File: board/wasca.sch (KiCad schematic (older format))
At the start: 104 parts, among them CN1 CARTRIDGE_EDGE_CONNECTOR, CN2 TFP09-2-12B, CN3 Conn_02x02_Odd_Even, CN4 Conn_02x02_Odd_Even, CN5 Conn_02x03_Odd_Even, CN6 USB-MB-S, CN7 Conn_02x05_Odd_Even, SW1 Conn_01x03_Male, U1 74ALVC164245, U10 SN74LVC1T45DBV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

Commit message: Finalizing stuff for 1.4: cleanup, silkscreen, comments etc.
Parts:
- removed CN6: USB-MB-S, con-usb-USB-MB-S, symbol USB-MB-S:USB-MB-S
- removed U13: ESP32_CAM, wasca:MODULE_ESP32-CAM, symbol esp32-devkitc:ESP32_CAM
- added CHAMFER_WARN1, CHAMFER_WARN2: CHAMFER_WARNING, wasca:CHAMFER_WARNING, symbol wasca:CHAMFER_WARNING
- added CN6: USB_C_Receptacle_USB2.0, wasca:DX07S016JA1R1500, symbol Connector:USB_C_Receptacle_USB2.0
- added R20: 5K1, Capacitor_SMD:C_0603_1608Metric_Pad1.08x0.95mm_HandSolder, symbol Device:R
- added U13: ESP32_CAM_HALF, wasca:MODULE_ESP32-CAM-HALF, symbol esp32-devkitc:ESP32_CAM_HALF
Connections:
- wire segments 878 -> 890
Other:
- note added: "Compatible connectors:\nHroparts TF-01A\nSOFNG TF-15x15\nSOFNG TF-015\nXUNPU TF-115K\nXUNPU TF-109\nHOAUC HYC77-TF09-200"
- note added: "Compatible connectors:\nJAE DX07S016JA1R1500\nJAE DX07S016JA3R1500\nHROPARTS TYPE-C-31-M-12\nHROPARTS TYPE-C-31-M-14\nXKB U262-161N-4BVC11\nJing Ext. C167321"
- note added: "Partially compatible\n(signals only)\n\nHirose DM3AT-SF-PEJM5\nKyocera 045138008100858+\nYamaichi PJS008-4100-0-VE"
- note removed: "TODO: add footprint to help orientation for 3V3 buffers\nTODO: pin B45 isn't A0 and consequently all address pins must be shifted and re-routed.\nTODO: restrict address lines count to A0-A23 (no plan to use A24)\nTODO: Use PLL output pin (32 or 33) for SDRAM clock. Probably requires to change SDRAM chip orientation.\nTODO: Change JTAG connector orientation, in order to support pokayoke connector.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"
- moved on the sheet: R13, R14

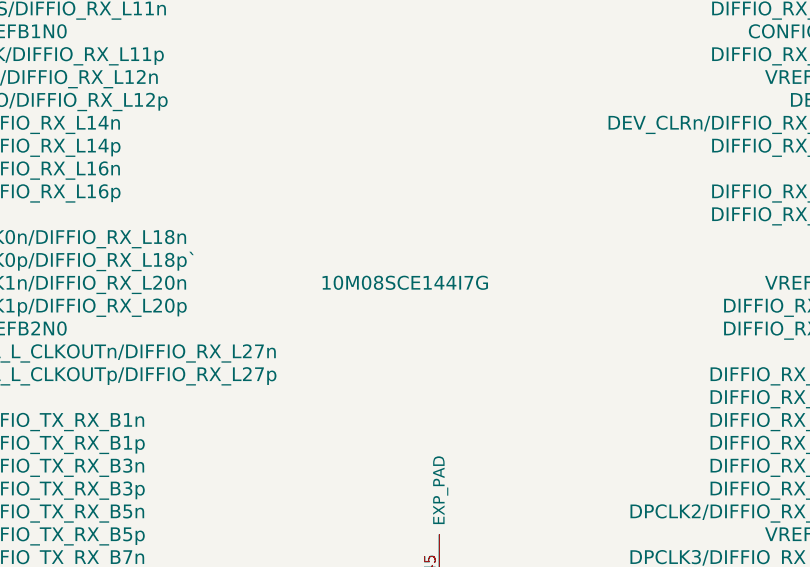
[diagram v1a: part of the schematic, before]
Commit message: Changing FPGA part to 10M08SCE144C8G. BOM recompilation.
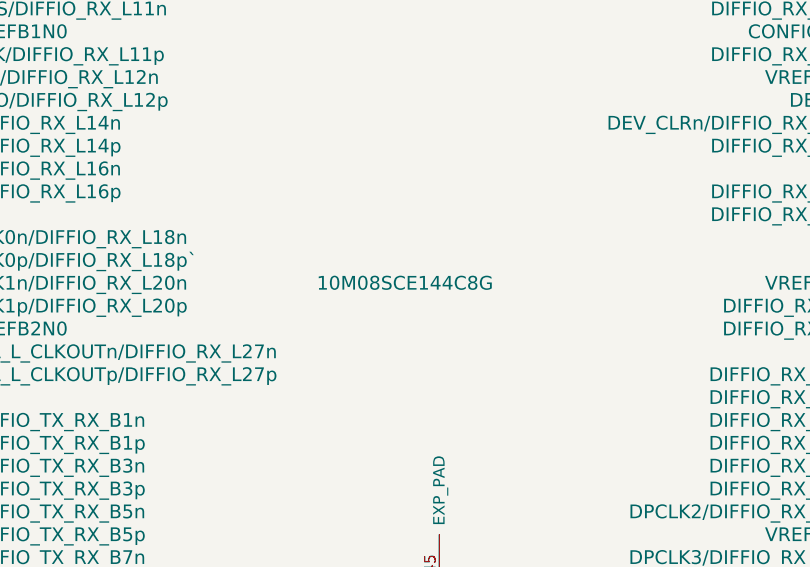
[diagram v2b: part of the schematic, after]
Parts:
- U3: value 10M08SCE144I7G -> 10M08SCE144C8G
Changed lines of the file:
@@
 P 25450 6500
 F 0 "U3" H 27500 9700 60  0000 C CNN
-F 1 "10M08SCE144I7G" H 25450 6800 60  0000 C CNN
+F 1 "10M08SCE144C8G" H 25450 6800 60  0000 C CNN
 F 2 "wasca:TQFP144_ALTERA_HANDSOLDERING" H 25450 6100 60  0001 C CNN
 F 3 "" H 25100 6500 60  0000 C CNN

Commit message: SSEL pin duplicated to STM32
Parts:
- added R21: 0, Capacitor_SMD:C_0603_1608Metric_Pad1.08x0.95mm_HandSolder, symbol Device:R
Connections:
- wire segments 890 -> 892

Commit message: Board 1.5 update (unchecked)
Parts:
- added R22, R23: 0, Capacitor_SMD:C_0603_1608Metric_Pad1.08x0.95mm_HandSolder, symbol Device:R
- added R24: 470, Capacitor_SMD:C_0603_1608Metric_Pad1.08x0.95mm_HandSolder, symbol Device:R
- SW1: footprint wasca:NINJA_SW -> Connector_PinHeader_2.54mm:PinHeader_1x03_P2.54mm_Vertical
- U6: footprint Package_QFP:LQFP-64_10x10mm_P0.5mm -> wasca:LQFP-64_10x10mm_P0.5mm
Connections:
- net labels added: 5V_SATURN_DETECT, BUFFERS_OE
- net labels removed: SPARE1, SPARE2
- wire segments 892 -> 889
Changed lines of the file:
@@
 Text Label 26400 14900 0    40   ~ 0
 LED3
-Text Label 26350 15000 0    40   ~ 0
-SPARE1
-Text Label 26350 15100 0    40   ~ 0
-SPARE2
 Text Notes 17850 10300 0    39   ~ 0
 SDRAM : shares 3V3 with MAX10\nDDR : requires 2V5 power supply
@@
 L power:GND #PWR065
 U 1 1 577FA6A0
-P 30050 15100
-F 0 "#PWR065" H 30050 14850 50  0001 C CNN
-F 1 "GND" H 30050 14950 50  0001 C CNN
-F 2 "" H 30050 15100 60  0000 C CNN
-F 3 "" H 30050 15100 60  0000 C CNN
-	1    30050 15100
+P 30400 15050
+F 0 "#PWR065" H 30400 14800 50  0001 C CNN
+F 1 "GND" H 30400 14900 50  0001 C CNN
+F 2 "" H 30400 15050 60  0000 C CNN
+F 3 "" H 30400 15050 60  0000 C CNN
+	1    30400 15050
 	1    0    0    -1
 $EndComp
@@
 	22450 2400 22600 2400
 Wire Wire Line
-	10150 3000 10250 3000
-Wire Wire Line
-	10150 3100 10250 3100
-Wire Wire Line
-	10250 3100 10250 3000
-Connection ~ 10250 3000
-Wire Wire Line
 	28850 4300 29250 4300
 Wire Wire Line
@@
 Connection ~ 16150 12050
 Wire Wire Line
-	9200 6950 9300 6950
-Wire Wire Line
 	22450 2900 23750 2900
 Wire Wire Line
@@
 Wire Wire Line
 	3650 14950 4400 14950
-Connection ~ 10250 1900
-Wire Wire Line
-	10250 2000 10250 1900
-Wire Wire Line
-	10150 2000 10250 2000
-Wire Wire Line
-	10150 1900 10250 1900
 Wire Wire Line
 	10150 3900 10900 3900
@@
 	18900 9950 17800 9950
 Wire Wire Line
-	29000 14900 30050 14900
+	29000 14900 30400 14900
 Wire Wire Line
-	30050 14900 30050 15000
+	30400 14900 30400 15000
 Wire Wire Line
-	29000 15000 30050 15000
-Connection ~ 30050 15000
+	29000 15000 30400 15000
+Connection ~ 30400 15000
 Wire Wire Line
 	15600 17300 15600 17450
@@
 	24750 2900 24850 2900
 Wire Wire Line
-	10250 3000 10850 3000
-Wire Wire Line
 	16150 12050 16550 12050
 Wire Wire Line
@@
 	8550 1600 8650 1600
 Wire Wire Line
-	10250 1900 10850 1900
-Wire Wire Line
 	9300 5550 10050 5550
 Wire Wire Line
@@
 	18250 9400 18600 9400
 Wire Wire Line
-	30050 15000 30050 15100
+	30400 15000 30400 15050
 Wire Wire Line
 	15600 17450 15600 17600
@@
 F 0 "U6" H 26000 11650 50  0000 C CNN
 F 1 "STM32F446RETx" H 26100 11500 50  0000 C CNN
-F 2 "Package_QFP:LQFP-64_10x10mm_P0.5mm" H 24900 11800 50  0001 R CNN
+F 2 "wasca:LQFP-64_10x10mm_P0.5mm" H 24900 11800 50  0001 R CNN
 F 3 "http://www.st.com/st-web-ui/static/active/en/resource/technical/document/datasheet/DM00141306.pdf" H 25500 13500 50  0001 C CNN
 	1    25500 13500
@@
 Wire Wire Line
 	9200 10800 10650 10800
-$Comp
-L power:GND #PWR047
-U 1 1 61E039AD
-P 9350 12000
-F 0 "#PWR047" H 9350 11750 50  0001 C CNN
-F 1 "GND" H 9350 11850 50  0000 C CNN
-F 2 "" H 9350 12000 60  0000 C CNN
-F 3 "" H 9350 12000 60  0000 C CNN
-	1    9350 12000
-	1    0    0    -1
-$EndComp
-Wire Wire Line
-	9200 12000 9350 12000
-$Comp
-L power:GND #PWR040
-U 1 1 61FB8A1A
-P 9350 10900
-F 0 "#PWR040" H 9350 10650 50  0001 C CNN
-F 1 "GND" H 9350 10750 50  0000 C CNN
-F 2 "" H 9350 10900 60  0000 C CNN
-F 3 "" H 9350 10900 60  0000 C CNN
-	1    9350 10900
-	1    0    0    -1
-$EndComp
-Wire Wire Line
-	9200 10900 9350 10900
 Wire Wire Line
 	9200 7550 10900 7550
@@
 Wire Wire Line
 	9200 7450 10900 7450
-Wire Wire Line
-	9200 7050 9300 7050
-Wire Wire Line
-	9300 7050 9300 6950
-Connection ~ 9300 6950
-Wire Wire Line
-	9300 6950 10800 6950
 $Comp
 L power:GND #PWR027
@@
 	1    0    0    -1
 $EndComp
-Wire Wire Line
-	9200 5850 9300 5850
-Wire Wire Line
-	9200 5950 9300 5950
-Wire Wire Line
-	9300 5950 9300 5850
-Connection ~ 9300 5850
-Wire Wire Line
-	9300 5850 10800 5850
 Text Label 11000 2400 0    40   ~ 0
 ABUS_3V_A1
@@
 DBG_UART_RX
 Wire Wire Line
-	29000 15100 29750 15100
-Text Label 29200 15100 0    40   ~ 0
+	29000 15100 29550 15100
+Text Label 29050 15100 0    40   ~ 0
 DBG_UART_TX
 Wire Wire Line
@@
 Text Label 27950 15100 0    40   ~ 0
 DBG_UART_RX
-Text Label 28200 15000 0    40   ~ 0
-SPARE1
-Text Label 28200 14900 0    40   ~ 0
-SPARE2
 Wire Wire Line
 	28500 15000 28100 15000
@@
 F 0 "SW1" H 23258 12481 50  0000 C CNN
 F 1 "Conn_01x03_Male" H 23258 12390 50  0000 C CNN
-F 2 "wasca:NINJA_SW" H 23150 12200 50  0001 C CNN
+F 2 "Connector_PinHeader_2.54mm:PinHeader_1x03_P2.54mm_Vertical" H 23150 12200 50  0001 C CNN
 F 3 "~" H 23150 12200 50  0001 C CNN
 	1    23150 12200
@@
 Wire Wire Line
 	26200 14100 27200 14100
-Wire Bus Line
-	2150 1400 2150 5850
-Wire Bus Line
-	6200 8300 6200 10600
-Wire Bus Line
-	3150 8300 3150 10600
-Wire Bus Line
-	6850 10600 6850 12900
-Wire Bus Line
-	6850 5350 6850 7750
-Wire Bus Line
-	6200 5450 6200 7500
-Wire Bus Line
-	2950 5850 2950 7700
-Wire Bus Line
-	7800 1400 7800 3800
 $Bitmap
 Pos 21400 14350
@@
 EndData
 $EndBitmap
+Text Label 27100 15100 0    40   ~ 0
+JTAG_TDO
+Wire Wire Line
+	27050 15100 27450 15100
+$Comp
+L Device:R R22
+U 1 1 6136C959
+P 27600 15100
+F 0 "R22" V 27680 15100 50  0000 C CNN
+F 1 "0" V 27500 15100 50  0000 C CNN
+F 2 "Capacitor_SMD:C_0603_1608Metric_Pad1.08x0.95mm_HandSolder" V 27530 15100 30  0001 C CNN
+F 3 "" H 27600 15100 30  0000 C CNN
+	1    27600 15100
+	0    1    -1   0
+$EndComp
+Text Label 28200 15000 0    40   ~ 0
+JTAG_TMS
+Text Label 28200 14900 0    40   ~ 0
+JTAG_TCK
+Wire Wire Line
+	29850 15100 30250 15100
+$Comp
+L Device:R R23
+U 1 1 61B604ED
+P 29700 15100
+F 0 "R23" V 29780 15100 50  0000 C CNN
+F 1 "0" V 29600 15100 50  0000 C CNN
+F 2 "Capacitor_SMD:C_0603_1608Metric_Pad1.08x0.95mm_HandSolder" V 29630 15100 30  0001 C CNN
+F 3 "" H 29700 15100 30  0000 C CNN
+	1    29700 15100
+	0    1    -1   0
+$EndComp
+Text Label 29950 15100 0    40   ~ 0
+JTAG_TDI
+Text Label 26350 15100 0    40   ~ 0
+JTAG_TCK
+Text Label 26350 15000 0    40   ~ 0
+JTAG_TMS
+Wire Wire Line
+	10150 1900 10850 1900
+Wire Wire Line
+	10150 3000 10850 3000
+Wire Wire Line
+	9200 5850 10800 5850
+Wire Wire Line
+	9200 6950 10800 6950
+$Comp
+L power:GND #PWR0106
+U 1 1 610023A1
+P 7700 6050
+F 0 "#PWR0106" H 7700 5800 50  0001 C CNN
+F 1 "GND" H 7700 5900 50  0001 C CNN
+F 2 "" H 7700 6050 60  0000 C CNN
+F 3 "" H 7700 6050 60  0000 C CNN
+	1    7700 6050
+	1    0    0    -1
+$EndComp
+Text Label 9400 5950 0    40   ~ 0
+BUFFERS_OE
+Wire Wire Line
+	9200 5950 9950 5950
+Text Label 9400 7050 0    40   ~ 0
+BUFFERS_OE
+Wire Wire Line
+	9200 7050 9950 7050
+Text Label 10350 2000 0    40   ~ 0
+BUFFERS_OE
+Wire Wire Line
+	10150 2000 10900 2000
+Text Label 10350 3100 0    40   ~ 0
+BUFFERS_OE
+Wire Wire Line
+	10150 3100 10900 3100
+Text Label 9400 10900 0    40   ~ 0
+BUFFERS_OE
+Wire Wire Line
+	9200 10900 9950 10900
+Text Label 9400 12000 0    40   ~ 0
+BUFFERS_OE
+Wire Wire Line
+	9200 12000 9950 12000
+Text Label 26400 12200 0    40   ~ 0
+BUFFERS_OE
+Wire Wire Line
+	26200 12200 26950 12200
+$Comp
+L Device:R R24
+U 1 1 619FFABF
+P 27350 12300
+F 0 "R24" V 27430 12300 50  0000 C CNN
+F 1 "470" V 27250 12300 50  0000 C CNN
+F 2 "Capacitor_SMD:C_0603_1608Metric_Pad1.08x0.95mm_HandSolder" V 27280 12300 30  0001 C CNN
+F 3 "" H 27350 12300 30  0000 C CNN
+	1    27350 12300
+	0    1    -1   0
+$EndComp
+Wire Wire Line
+	27200 12300 26200 12300
+Wire Wire Line
+	27500 12300 28400 12300
+Text Label 28200 12300 2    40   ~ 0
++5V_SATURN
+Wire Bus Line
+	2150 1400 2150 5850
+Wire Bus Line
+	6200 8300 6200 10600
+Wire Bus Line
+	3150 8300 3150 10600
+Wire Bus Line
+	6850 10600 6850 12900
+Wire Bus Line
+	6850 5350 6850 7750
+Wire Bus Line
+	6200 5450 6200 7500
+Wire Bus Line
+	2950 5850 2950 7700
+Wire Bus Line
+	7800 1400 7800 3800
+Text Label 26850 12300 2    40   ~ 0
+5V_SATURN_DETECT
 $EndSCHEMATC

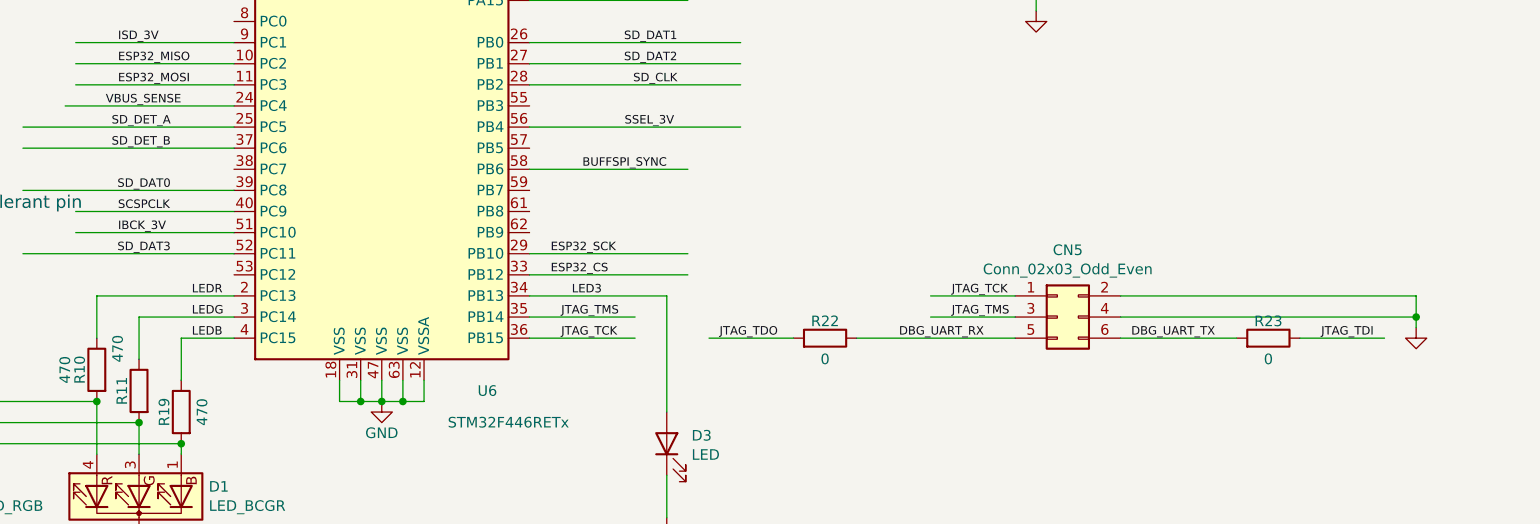
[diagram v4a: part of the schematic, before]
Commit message: Board 1.5 , STM-to-MAX JTAG detached from UART
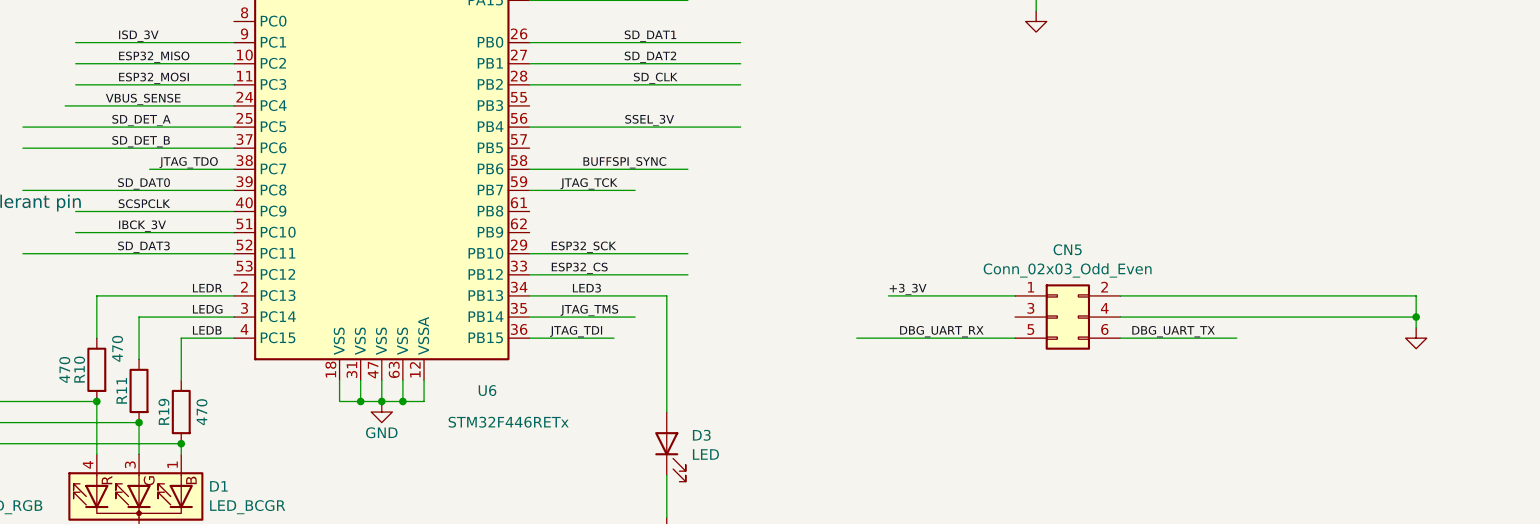
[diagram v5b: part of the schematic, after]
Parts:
- removed R22, R23: 0, Capacitor_SMD:C_0603_1608Metric_Pad1.08x0.95mm_HandSolder, symbol Device:R
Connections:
- wire segments 889 -> 888
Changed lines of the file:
@@
 	26200 15000 26700 15000
 Wire Wire Line
-	26200 15100 26700 15100
-Wire Wire Line
-	28500 14900 28100 14900
+	26200 14400 26700 14400
 Wire Wire Line
 	25700 11550 26300 11550
@@
 Text Label 27950 15100 0    40   ~ 0
 DBG_UART_RX
-Wire Wire Line
-	28500 15000 28100 15000
 $Comp
 L Device:LED_BCGR D1
@@
 EndData
 $EndBitmap
-Text Label 27100 15100 0    40   ~ 0
+Text Label 24450 14300 0    40   ~ 0
 JTAG_TDO
 Wire Wire Line
-	27050 15100 27450 15100
-$Comp
-L Device:R R22
-U 1 1 6136C959
-P 27600 15100
-F 0 "R22" V 27680 15100 50  0000 C CNN
-F 1 "0" V 27500 15100 50  0000 C CNN
-F 2 "Capacitor_SMD:C_0603_1608Metric_Pad1.08x0.95mm_HandSolder" V 27530 15100 30  0001 C CNN
-F 3 "" H 27600 15100 30  0000 C CNN
-	1    27600 15100
-	0    1    -1   0
-$EndComp
-Text Label 28200 15000 0    40   ~ 0
-JTAG_TMS
-Text Label 28200 14900 0    40   ~ 0
-JTAG_TCK
+	24400 14300 24800 14300
 Wire Wire Line
-	29850 15100 30250 15100
-$Comp
-L Device:R R23
-U 1 1 61B604ED
-P 29700 15100
-F 0 "R23" V 29780 15100 50  0000 C CNN
-F 1 "0" V 29600 15100 50  0000 C CNN
-F 2 "Capacitor_SMD:C_0603_1608Metric_Pad1.08x0.95mm_HandSolder" V 29630 15100 30  0001 C CNN
-F 3 "" H 29700 15100 30  0000 C CNN
-	1    29700 15100
-	0    1    -1   0
-$EndComp
-Text Label 29950 15100 0    40   ~ 0
+	26200 15100 26600 15100
+Text Label 26300 15100 0    40   ~ 0
 JTAG_TDI
-Text Label 26350 15100 0    40   ~ 0
+Text Label 26350 14400 0    40   ~ 0
 JTAG_TCK
 Text Label 26350 15000 0    40   ~ 0
@@
 Text Label 28200 12300 2    40   ~ 0
 +5V_SATURN
+Text Label 26850 12300 2    40   ~ 0
+5V_SATURN_DETECT
+Text Label 27900 14900 0    40   ~ 0
++3_3V
+Wire Wire Line
+	27900 14900 28500 14900
 Wire Bus Line
 	2150 1400 2150 5850
@@
 Wire Bus Line
 	7800 1400 7800 3800
-Text Label 26850 12300 2    40   ~ 0
-5V_SATURN_DETECT
 $EndSCHEMATC

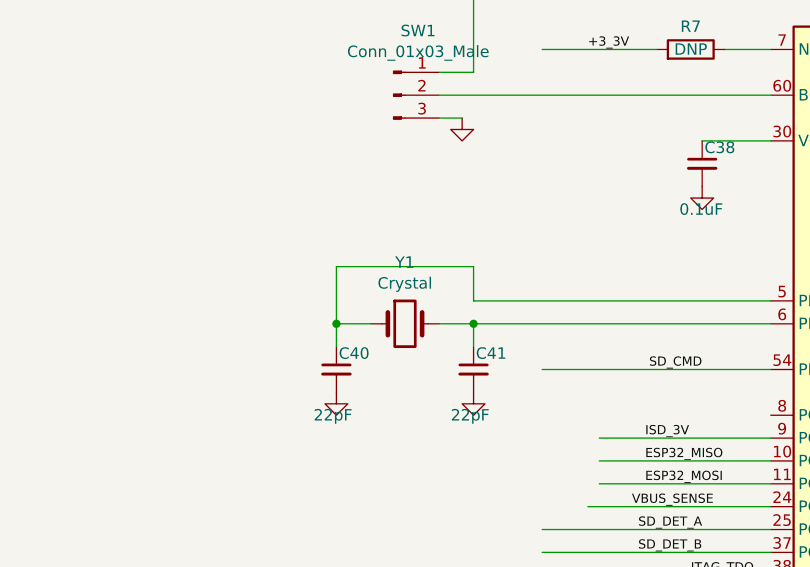
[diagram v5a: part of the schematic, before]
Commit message: BOM generated. Crystal value updated.
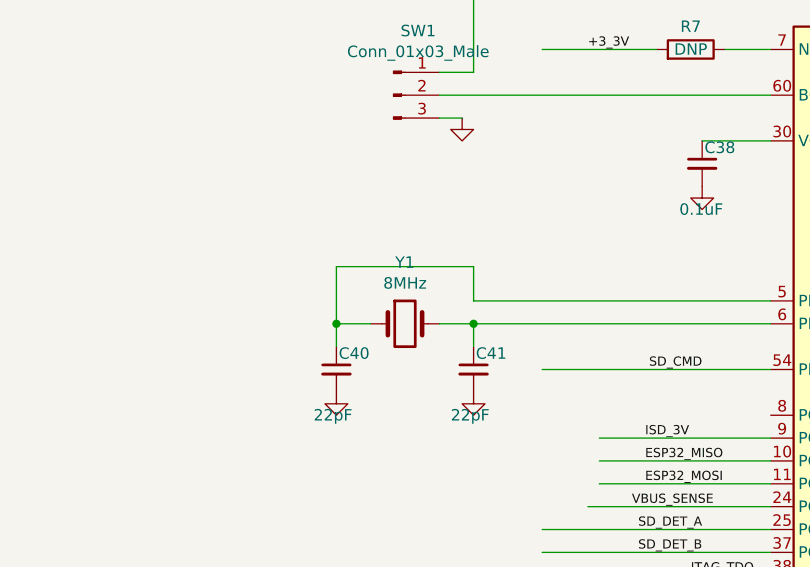
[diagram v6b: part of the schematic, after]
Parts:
- Y1: value Crystal -> 8MHz
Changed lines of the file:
@@
 P 23200 13200
 F 0 "Y1" H 23200 13468 50  0000 C CNN
-F 1 "Crystal" H 23200 13377 50  0000 C CNN
+F 1 "8MHz" H 23200 13377 50  0000 C CNN
 F 2 "Crystal:Crystal_HC49-4H_Vertical" H 23200 13200 50  0001 C CNN
 F 3 "~" H 23200 13200 50  0001 C CNN
